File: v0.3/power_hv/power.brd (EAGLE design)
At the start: 86.5 x 50.8 mm, 56 parts, among them IC1 ACS758ECB-200B-PFF-T, IC3 ACS758ECB-200B-PFF-T, Q1 FDB86135, Q10 FDB86135, Q11 FDB86135, Q12 FDB86135, Q2 FDB86135, Q3 FDB86135, Q4 FDB86135, Q5 FDB86135, Q6 FDB86135, Q7 FDB86135, Q8 FDB86135, Q9 FDB86135

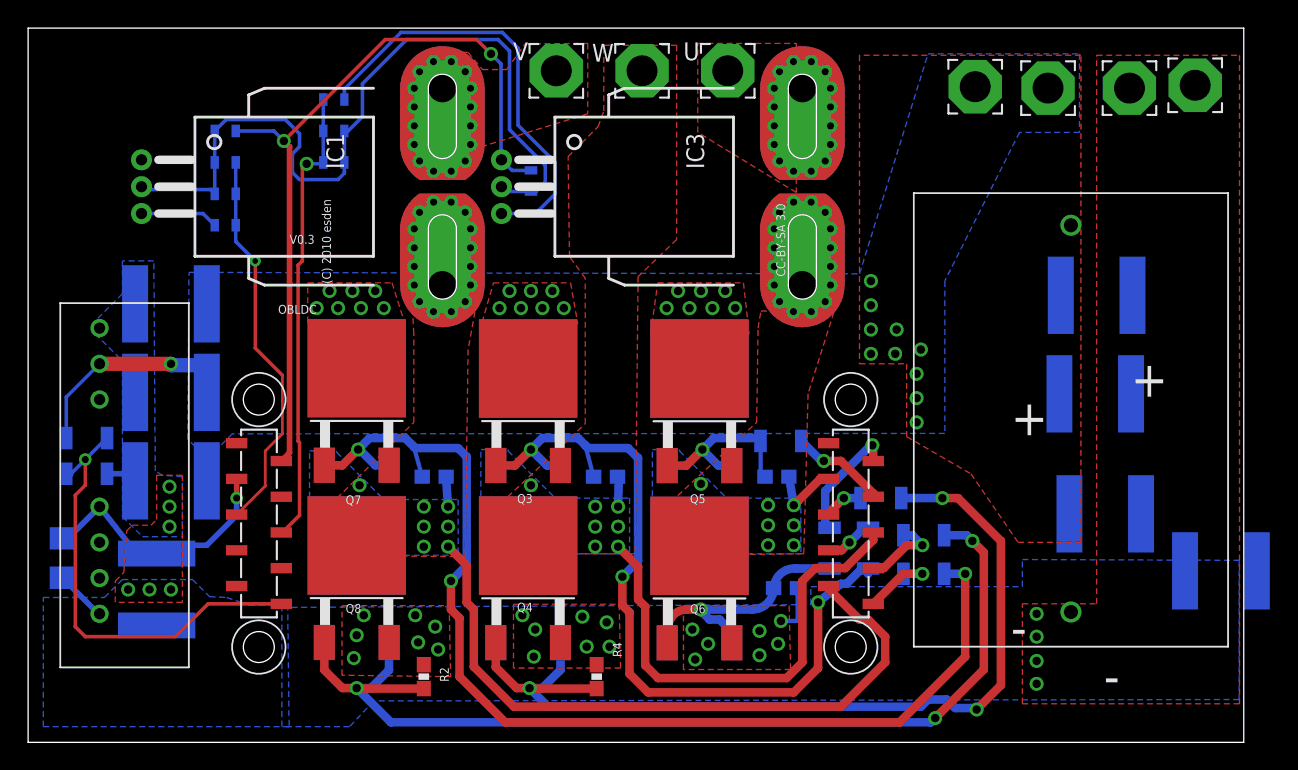
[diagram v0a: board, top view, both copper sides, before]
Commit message: TODO: Route ground connection to driver board.
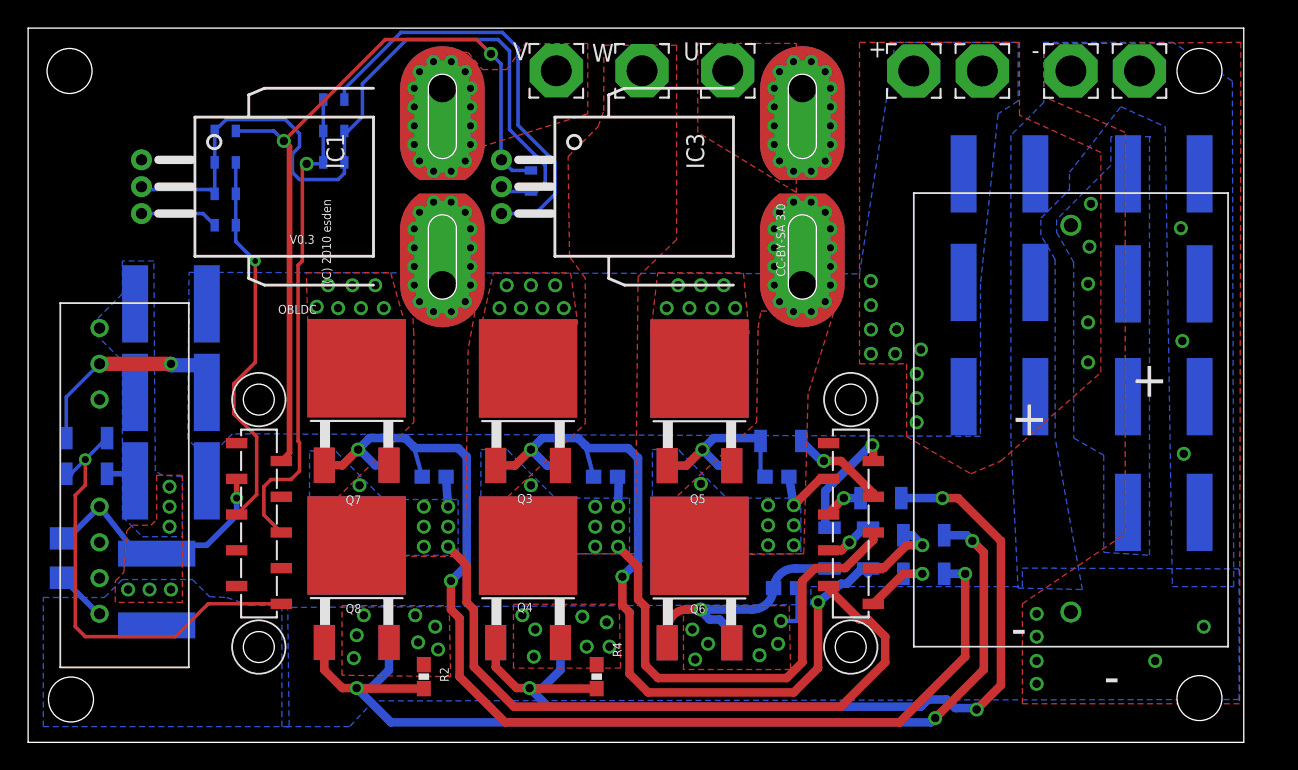
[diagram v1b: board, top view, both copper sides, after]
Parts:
- added C16, C17, C18: (no value), rcl:C2220K
- moved C12 28.5 mm to (67.6, 35.4)
- moved C11 11.2 mm to (55.9, 19.5)
- moved C9 11.1 mm to (55.9, 35.4)
- moved C10 10.4 mm to (55.9, 27.6)
- moved PAD_VCC1 4.83 mm to (54.7, 42.7)
- moved PAD_VCC 4.51 mm to (49.8, 42.7)
- moved PAD_GND 4.34 mm to (61.0, 42.7)
- moved PAD_GND1 4.09 mm to (65.8, 42.7)
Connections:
- net GND: now also C16.2, C17.2, C18.2
- net VCC: now also C16.1, C17.1, C18.1
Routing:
- net U_CURRENT: track 32.8 -> 34.7 mm
- net VCC: vias 32 -> 38
- net GND: vias 31 -> 36
